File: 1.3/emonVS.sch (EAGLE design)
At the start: 46 parts, among them CN1 TERMINAL_BLOCK_5P, CN2 RJ45 Jack, CN3 TERMINAL_BLOCK_2P, T1 ZMPT101B, T2 ZMPT101B, T3 ZMPT101B

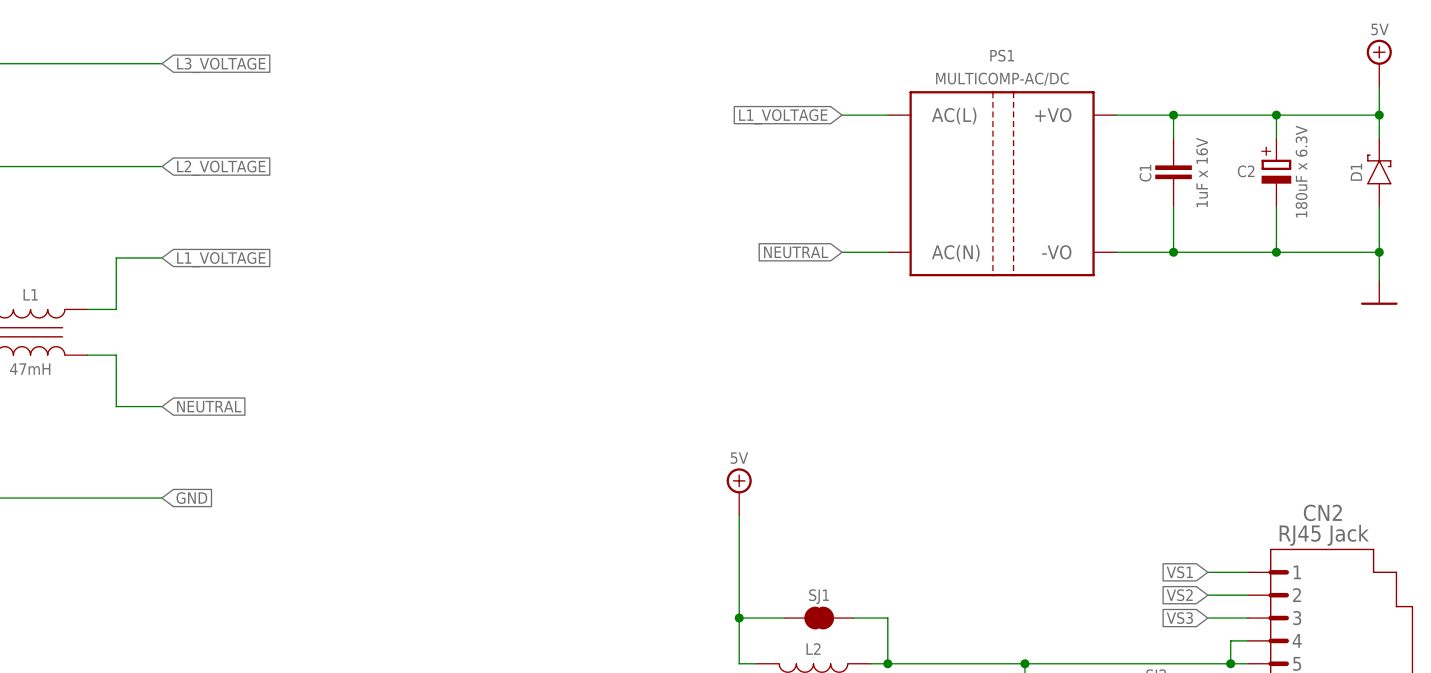
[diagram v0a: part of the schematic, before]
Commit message: minor improvement: added D1 value
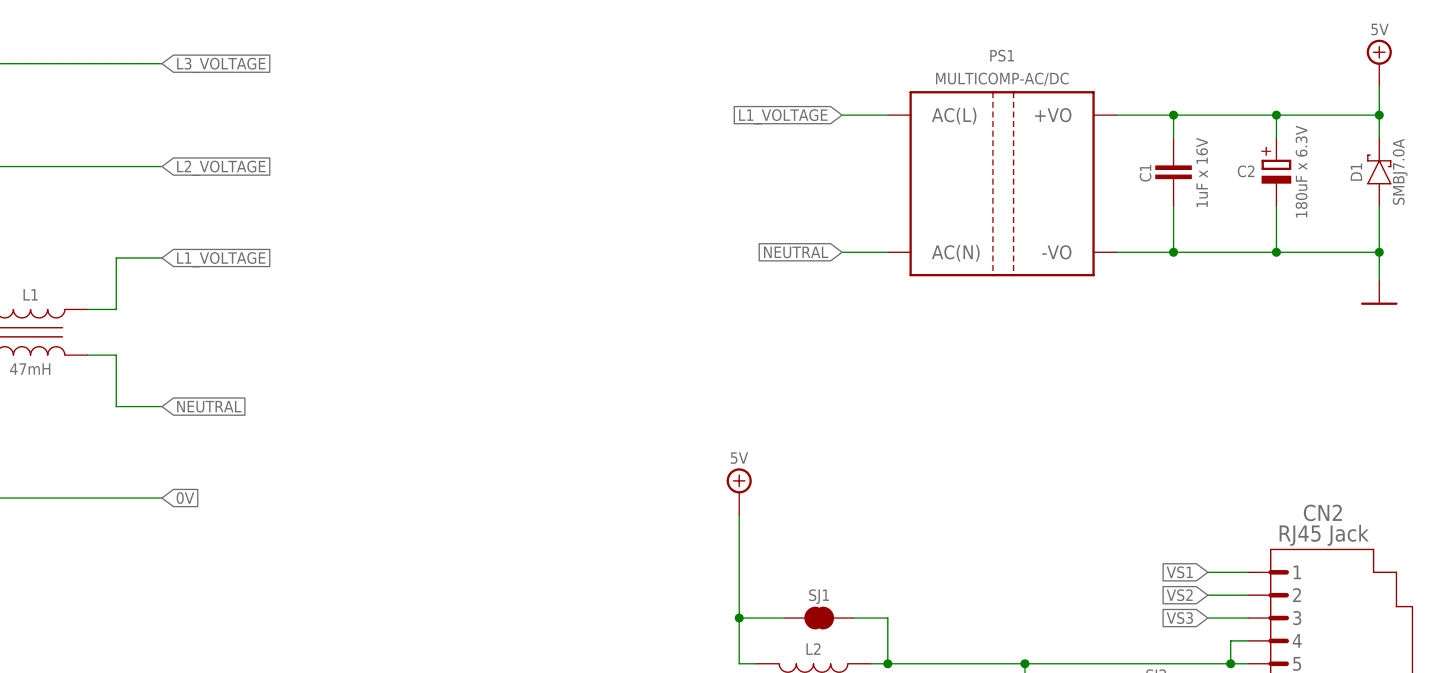
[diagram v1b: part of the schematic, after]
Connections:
- net GND renamed 0V

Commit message: Added PN attribute to all parts
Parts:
- C3: PN (none) -> B32923C3105M000
- PS1: PN (none) -> MP-LD05-23B05R2
- R1, R10, R12, R13, R14, R15, R16, R17, R19, R2, R20, R21, R3, R5, R6, R7, R8, R9: PN (none) -> ERJ-H3GJ103V
- R11, R18, R4: PN (none) -> ERJ-H3EF75R0V

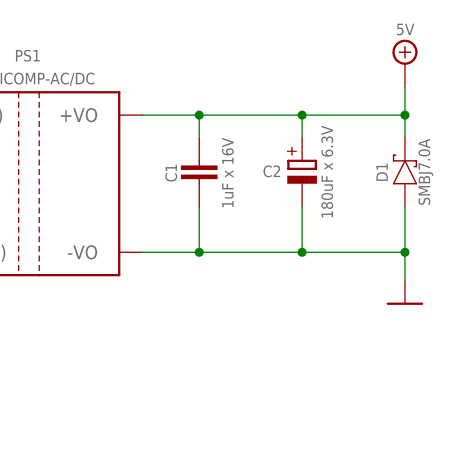
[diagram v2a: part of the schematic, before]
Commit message: changed D1 symbol from schottky to TVS
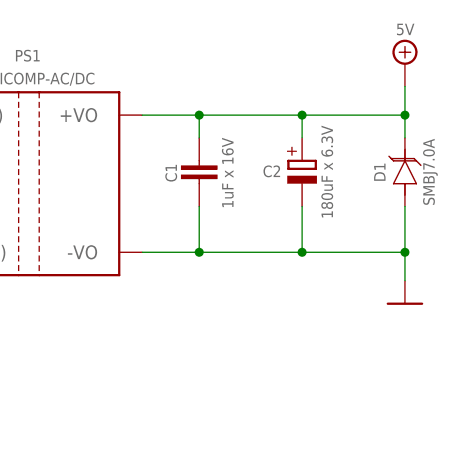
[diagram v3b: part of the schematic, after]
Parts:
- D1: value SCHOTTKY-SMBJ7.0A -> TVS; device My-Diodes:SCHOTTKY-SMBJ7.0A -> My-Diodes:TVS
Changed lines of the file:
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@@
 <attribute name="PN" value="6SVPE180M"/>
 </part>
-<part name="D1" library="My-Diodes" library_urn="urn:adsk.eagle:library:35512051" deviceset="SCHOTTKY-" device="SMBJ7.0A" package3d_urn="urn:adsk.eagle:package:35541124/5"/>
+<part name="D1" library="My-Diodes" library_urn="urn:adsk.eagle:library:35512051" deviceset="TVS" device="" package3d_urn="urn:adsk.eagle:package:35541124/5"/>
 <part name="FD1" library="OpenEnergyMonitor" deviceset="FIDUCIAL" device="1X2"/>
 <part name="FD2" library="OpenEnergyMonitor" deviceset="FIDUCIAL" device="1X2"/>
@@
 </instance>
 <instance part="D1" gate="G$1" x="249.555" y="151.13" smashed="yes" rot="R90" grouprefs="EMBEDDED_POWER_SUPPLY">
-<attribute name="NAME" x="247.015" y="151.13" size="1.27" layer="95" rot="R90" align="center"/>
-<attribute name="FAMILY" x="251.714" y="151.13" size="1.27" layer="96" rot="R90" align="center"/>
+<attribute name="NAME" x="246.761" y="151.13" size="1.27" layer="95" rot="R90" align="center"/>
+<attribute name="FAMILY" x="252.222" y="151.13" size="1.27" layer="96" rot="R90" align="center"/>
 </instance>
 <instance part="FD1" gate="G$1" x="149.225" y="3.175" smashed="yes" rot="R90"/>
